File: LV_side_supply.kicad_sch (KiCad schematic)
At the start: 16 parts, among them U201 AMS1117-3.3

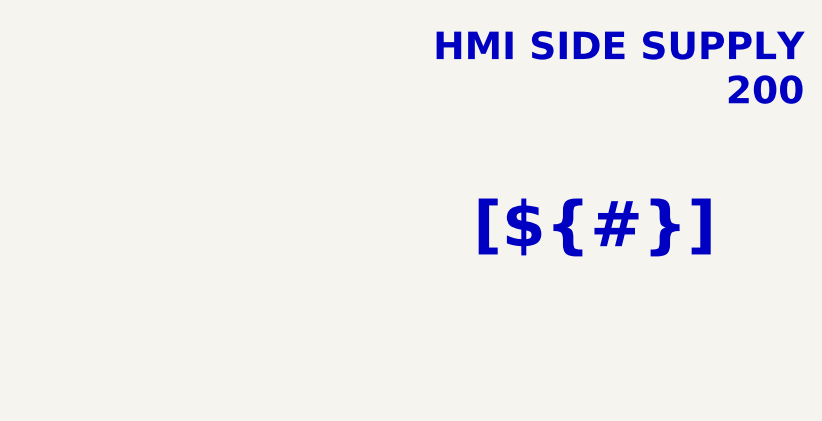
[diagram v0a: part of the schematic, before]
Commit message: Reworked sheet titles
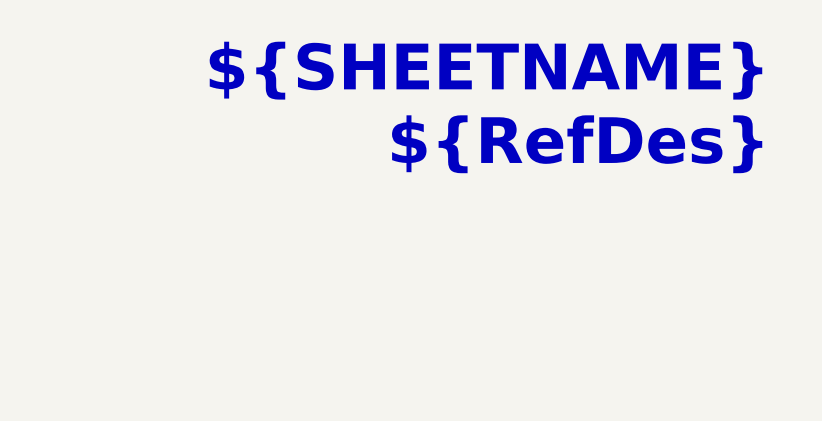
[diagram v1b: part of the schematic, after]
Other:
- note removed: "HMI SIDE SUPPLY 200"
- title: (none) -> ${SHEETNAME}
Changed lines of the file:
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@@
 	(paper "A4")
 	(title_block
+		(title "${SHEETNAME}")
 		(date "2025-01-12")
 	)
@@
 		(fill
 			(type none)
-		)
-	)
-	(text "HMI SIDE SUPPLY\n200"
-		(exclude_from_sim no)
-		(at 283.21 19.05 0)
-		(effects
-			(font
-				(size 3.048 3.048)
-				(thickness 0.4064)
-				(bold yes)
-				(color 0 0 255 1)
-			)
-			(justify right)
 		)
 	)
@@
 		)
 	)
-	(text_box "[${#}] ${TITLE}"
+	(text_box "${SHEETNAME}\n${RefDes}"
 		(exclude_from_sim no)
-		(at 177.8 29.845 0)
-		(size 101.6 12.7)
-		(margins 5.9999 5.9999 5.9999 5.9999)
+		(at 228.6 15.24 0)
+		(size 53.34 15.24)
+		(margins 2.54 1.27 2.54 1.27)
 		(stroke
 			(width -0.0001)

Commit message: Added PCB
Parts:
- PS201: footprint Personal:DCDC_converter_Hilink -> Personal:Hilink_no_courtyard
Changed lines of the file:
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@@
 	(title_block
 		(title "${SHEETNAME}")
-		(date "2025-01-12")
+		(date "2025-07-04")
 	)
 	(rectangle
@@
 		(at 228.6 15.24 0)
 		(size 53.34 15.24)
-		(margins 2.54 1.27 2.54 1.27)
+		(margins 1.27 1.27 1.27 1.27)
 		(stroke
 			(width -0.0001)
@@
 			)
 		)
-		(property "Description" ""
+		(property "Description" "Local power symbol (sink), cosmetic use only"
 			(at 73.66 44.45 0)
 			(effects
@@
 			)
 		)
-		(property "Footprint" "Personal:DCDC_converter_Hilink"
+		(property "Footprint" "Personal:Hilink_no_courtyard"
 			(at 93.98 50.8 0)
 			(effects
@@
 			)
 		)
-		(property "Description" ""
+		(property "Description" "Local power symbol (source), cosmetic use only"
 			(at 115.57 39.37 0)
 			(effects
@@
 			)
 		)
-		(property "Description" ""
+		(property "Description" "Local power symbol (sink), cosmetic use only"
 			(at 76.2 39.37 0)
 			(effects
@@
 			)
 		)
-		(property "Description" ""
+		(property "Description" "Local power symbol (source), cosmetic use only"
 			(at 33.02 24.13 0)
 			(effects
@@
 			)
 		)
-		(property "Description" ""
+		(property "Description" "Local power symbol (source), cosmetic use only"
 			(at 149.86 39.37 0)
 			(effects
@@
 			)
 		)
-		(property "Description" ""
+		(property "Description" "Local power symbol (sink), cosmetic use only"
 			(at 33.02 39.37 0)
 			(effects
@@
 			)
 		)
-		(property "Description" ""
+		(property "Description" "Local power symbol (source), cosmetic use only"
 			(at 33.02 31.75 0)
 			(effects

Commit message: Readme updated
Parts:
- PS201: footprint Personal:Hilink_no_courtyard -> Converter_ACDC:Converter_ACDC_Hi-Link_HLK-5Mxx
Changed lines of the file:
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@@
 			)
 		)
-		(property "Footprint" "Personal:Hilink_no_courtyard"
+		(property "Footprint" "Converter_ACDC:Converter_ACDC_Hi-Link_HLK-5Mxx"
 			(at 93.98 50.8 0)
 			(effects

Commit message: updating BOM info
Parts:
- C201: Manufacturer (none) -> Generic
- C202: Manufacturer (none) -> CCTC; Manufacturer Part Number (none) -> TCC0603X7R104K500CT
- PS201: Manufacturer (none) -> Hilink; Manufacturer Part Number (none) -> HLK-5M05
- U201: Manufacturer (none) -> UMW; Manufacturer Part Number (none) -> AMS1117-3.3

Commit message: Checked. Preparing release
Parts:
- PS201: footprint Converter_ACDC:Converter_ACDC_Hi-Link_HLK-5Mxx -> Personal:Hilink_no_courtyard
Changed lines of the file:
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@@
 			)
 		)
-		(property "Footprint" "Converter_ACDC:Converter_ACDC_Hi-Link_HLK-5Mxx"
+		(property "Footprint" "Personal:Hilink_no_courtyard"
 			(at 93.98 50.8 0)
 			(effects
